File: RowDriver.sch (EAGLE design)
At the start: 9 parts, among them Q1 PBSS5160U

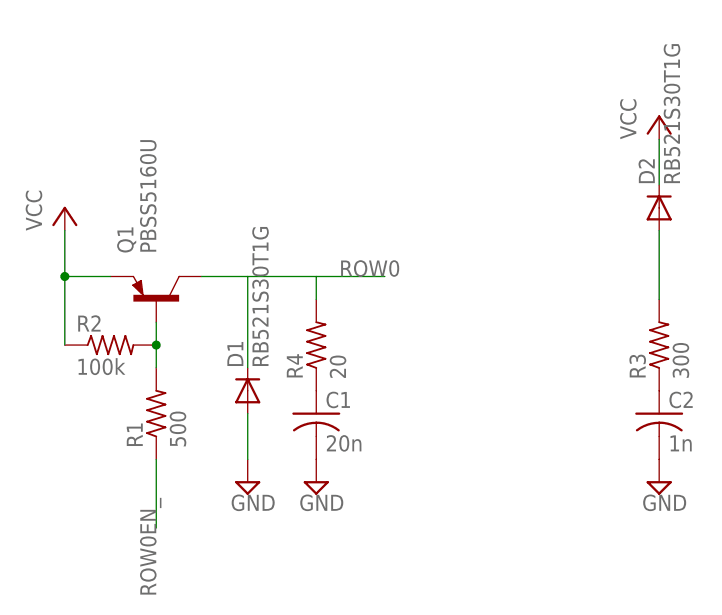
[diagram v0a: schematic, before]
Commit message: Created separate schematics for Row and Column Driver circuits. Added arrayed row and column noise filtering circuits. Added decoupling caps for ICs. Added voltage regulators for 3.3 and 5v rails. Added voltage regulators to parts library. Added values to LED driver current sense resistors.
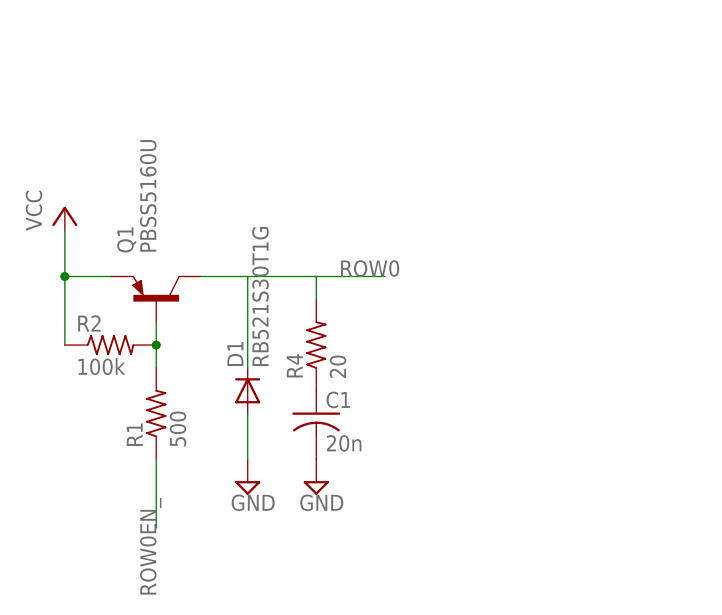
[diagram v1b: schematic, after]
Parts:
- removed C2: 1n, resistor:C-USC0805
- removed D2: RB521S30T1G, diode:DIODE-SOD523
- removed R3: 300, resistor:R-US_R0805
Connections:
- removed net N$5: D2.A, R3.2
- removed net N$6: C2.1, R3.1
- net GND: no longer C2.2
- net VCC: no longer D2.C
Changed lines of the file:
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@@
 <grid distance="0.1" unitdist="inch" unit="inch" style="lines" multiple="1" display="no" altdistance="0.01" altunitdist="inch" altunit="inch"/>
 <layers>
-<layer number="1" name="Top" color="4" fill="1" visible="yes" active="no"/>
-<layer number="16" name="Bottom" color="1" fill="1" visible="yes" active="no"/>
-<layer number="17" name="Pads" color="2" fill="1" visible="yes" active="no"/>
-<layer number="18" name="Vias" color="2" fill="1" visible="yes" active="no"/>
-<layer number="19" name="Unrouted" color="6" fill="1" visible="yes" active="no"/>
-<layer number="20" name="Dimension" color="15" fill="1" visible="yes" active="no"/>
-<layer number="21" name="tPlace" color="7" fill="1" visible="yes" active="no"/>
-<layer number="22" name="bPlace" color="7" fill="1" visible="yes" active="no"/>
-<layer number="23" name="tOrigins" color="15" fill="1" visible="yes" active="no"/>
-<layer number="24" name="bOrigins" color="15" fill="1" visible="yes" active="no"/>
-<layer number="25" name="tNames" color="7" fill="1" visible="yes" active="no"/>
-<layer number="26" name="bNames" color="7" fill="1" visible="yes" active="no"/>
-<layer number="27" name="tValues" color="7" fill="1" visible="yes" active="no"/>
-<layer number="28" name="bValues" color="7" fill="1" visible="yes" active="no"/>
+<layer number="1" name="Top" color="4" fill="1" visible="no" active="no"/>
+<layer number="16" name="Bottom" color="1" fill="1" visible="no" active="no"/>
+<layer number="17" name="Pads" color="2" fill="1" visible="no" active="no"/>
+<layer number="18" name="Vias" color="2" fill="1" visible="no" active="no"/>
+<layer number="19" name="Unrouted" color="6" fill="1" visible="no" active="no"/>
+<layer number="20" name="Dimension" color="15" fill="1" visible="no" active="no"/>
+<layer number="21" name="tPlace" color="7" fill="1" visible="no" active="no"/>
+<layer number="22" name="bPlace" color="7" fill="1" visible="no" active="no"/>
+<layer number="23" name="tOrigins" color="15" fill="1" visible="no" active="no"/>
+<layer number="24" name="bOrigins" color="15" fill="1" visible="no" active="no"/>
+<layer number="25" name="tNames" color="7" fill="1" visible="no" active="no"/>
+<layer number="26" name="bNames" color="7" fill="1" visible="no" active="no"/>
+<layer number="27" name="tValues" color="7" fill="1" visible="no" active="no"/>
+<layer number="28" name="bValues" color="7" fill="1" visible="no" active="no"/>
 <layer number="29" name="tStop" color="7" fill="3" visible="no" active="no"/>
 <layer number="30" name="bStop" color="7" fill="6" visible="no" active="no"/>
@@
 <layer number="35" name="tGlue" color="7" fill="4" visible="no" active="no"/>
 <layer number="36" name="bGlue" color="7" fill="5" visible="no" active="no"/>
-<layer number="37" name="tTest" color="7" fill="1" visible="yes" active="no"/>
-<layer number="38" name="bTest" color="7" fill="1" visible="yes" active="no"/>
+<layer number="37" name="tTest" color="7" fill="1" visible="no" active="no"/>
+<layer number="38" name="bTest" color="7" fill="1" visible="no" active="no"/>
 <layer number="39" name="tKeepout" color="4" fill="11" visible="no" active="no"/>
 <layer number="40" name="bKeepout" color="1" fill="11" visible="no" active="no"/>
@@
 <layer number="44" name="Drills" color="7" fill="1" visible="no" active="no"/>
 <layer number="45" name="Holes" color="7" fill="1" visible="no" active="no"/>
-<layer number="46" name="Milling" color="3" fill="1" visible="yes" active="no"/>
-<layer number="47" name="Measures" color="7" fill="1" visible="yes" active="no"/>
-<layer number="48" name="Document" color="7" fill="1" visible="yes" active="no"/>
-<layer number="49" name="Reference" color="7" fill="1" visible="yes" active="no"/>
-<layer number="51" name="tDocu" color="7" fill="1" visible="yes" active="no"/>
-<layer number="52" name="bDocu" color="7" fill="1" visible="yes" active="no"/>
+<layer number="46" name="Milling" color="3" fill="1" visible="no" active="no"/>
+<layer number="47" name="Measures" color="7" fill="1" visible="no" active="no"/>
+<layer number="48" name="Document" color="7" fill="1" visible="no" active="no"/>
+<layer number="49" name="Reference" color="7" fill="1" visible="no" active="no"/>
+<layer number="51" name="tDocu" color="7" fill="1" visible="no" active="no"/>
+<layer number="52" name="bDocu" color="7" fill="1" visible="no" active="no"/>
 <layer number="91" name="Nets" color="2" fill="1" visible="yes" active="yes"/>
 <layer number="92" name="Busses" color="1" fill="1" visible="yes" active="yes"/>
@@
 <part name="C1" library="resistor" deviceset="C-US" device="C0805" value="20n"/>
 <part name="P+1" library="supply1" deviceset="VCC" device=""/>
-<part name="SUPPLY4" library="supply2" deviceset="GND" device=""/>
-<part name="R3" library="resistor" deviceset="R-US_" device="R0805" value="300"/>
-<part name="C2" library="resistor" deviceset="C-US" device="C0805" value="1n"/>
-<part name="P+2" library="supply1" deviceset="VCC" device=""/>
 <part name="Q1" library="transistor" deviceset="*-PNP-" device="SOT23-BCE" value="PBSS5160U"/>
 <part name="D1" library="diode" deviceset="DIODE-" device="SOD523" value="RB521S30T1G"/>
-<part name="D2" library="diode" deviceset="DIODE-" device="SOD523" value="RB521S30T1G"/>
 </parts>
 <sheets>
@@
 <instance part="C1" gate="G$1" x="20.32" y="86.36"/>
 <instance part="P+1" gate="VCC" x="-7.62" y="109.22"/>
-<instance part="SUPPLY4" gate="GND" x="58.42" y="78.74"/>
-<instance part="R3" gate="G$1" x="58.42" y="93.98" rot="R90"/>
-<instance part="C2" gate="G$1" x="58.42" y="86.36"/>
-<instance part="P+2" gate="VCC" x="58.42" y="119.38"/>
 <instance part="Q1" gate="G$1" x="2.54" y="99.06" smashed="yes" rot="R90">
 <attribute name="NAME" x="0" y="104.14" size="1.778" layer="95" rot="R90"/>
@@
 </instance>
 <instance part="D1" gate="G$1" x="12.7" y="88.9" rot="R90"/>
-<instance part="D2" gate="G$1" x="58.42" y="109.22" rot="R90"/>
 </instances>
 <busses>
@@
 <pinref part="SUPPLY2" gate="GND" pin="GND"/>
 <pinref part="C1" gate="G$1" pin="2"/>
-</segment>
-<segment>
-<pinref part="SUPPLY4" gate="GND" pin="GND"/>
-<pinref part="C2" gate="G$1" pin="2"/>
 </segment>
 </net>
@@
 <pinref part="Q1" gate="G$1" pin="E"/>
 </segment>
-<segment>
-<pinref part="P+2" gate="VCC" pin="VCC"/>
-<wire x1="58.42" y1="116.84" x2="58.42" y2="111.76" width="0.1524" layer="91"/>
-<pinref part="D2" gate="G$1" pin="C"/>
-</segment>
 </net>
-<net name="N$5" class="0">
-<segment>
-<pinref part="R3" gate="G$1" pin="2"/>
-<wire x1="58.42" y1="106.68" x2="58.42" y2="99.06" width="0.1524" layer="91"/>
-<pinref part="D2" gate="G$1" pin="A"/>
-</segment>
-</net>
-<net name="N$6" class="0">
-<segment>
-<pinref part="R3" gate="G$1" pin="1"/>
-<pinref part="C2" gate="G$1" pin="1"/>
-</segment>
-</net>
